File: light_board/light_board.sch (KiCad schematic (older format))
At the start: 17 parts, among them J1 CONN_01X02, J2 Screw_Terminal_1x02, J3 Screw_Terminal_1x02, Q1 FDC658AP, U1 LM3409MY

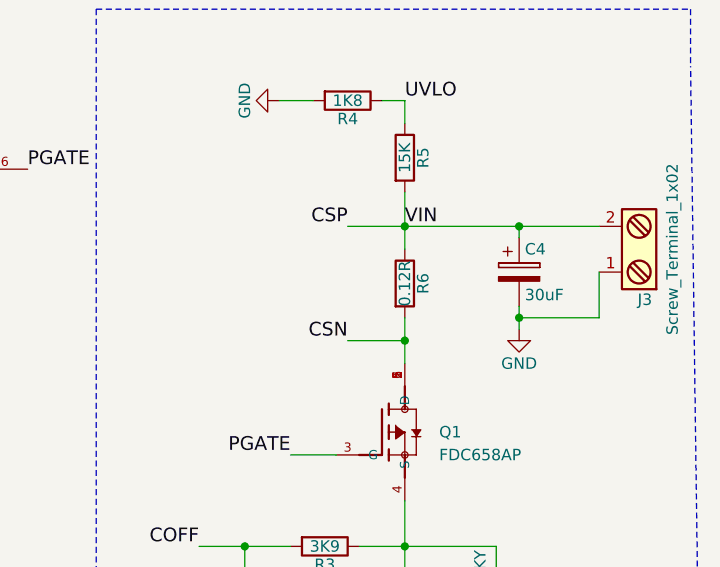
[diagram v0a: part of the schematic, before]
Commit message: changed design to use large resistor
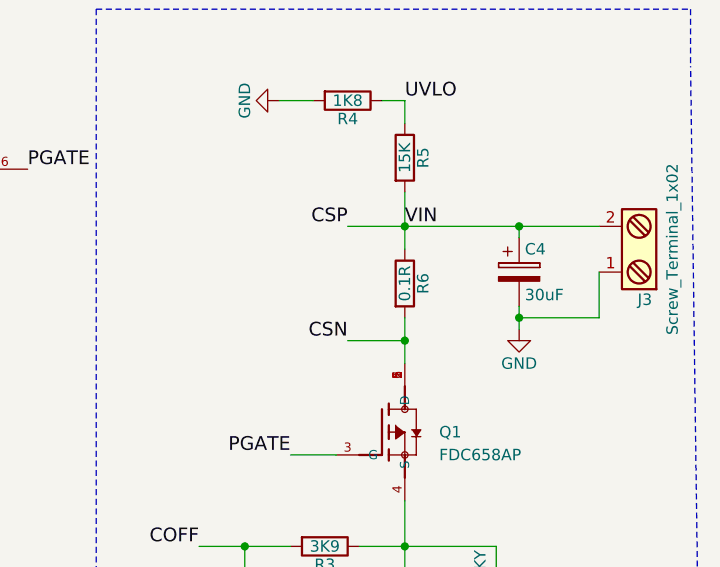
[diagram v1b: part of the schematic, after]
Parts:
- R6: value 0.12R -> 0.1R; footprint agg:0805 -> Resistors_THT:R_Axial_DIN0614_L14.3mm_D5.7mm_P15.24mm_Horizontal
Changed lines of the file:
@@
 P 8250 3300
 F 0 "R6" V 8330 3300 50  0000 C CNN
-F 1 "0.12R" V 8250 3300 50  0000 C CNN
-F 2 "agg:0805" V 8180 3300 50  0001 C CNN
+F 1 "0.1R" V 8250 3300 50  0000 C CNN
+F 2 "Resistors_THT:R_Axial_DIN0614_L14.3mm_D5.7mm_P15.24mm_Horizontal" V 8180 3300 50  0001 C CNN
 F 3 "" H 8250 3300 50  0001 C CNN
 	1    8250 3300
